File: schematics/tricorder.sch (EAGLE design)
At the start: 70 parts, among them IC1 EADOGM128, U1 V_REG_LDOSMD, U2 CY8C5XXX, U3 M05X2-0.05-SMD, U7 MICROUSB, Y1 XRCGB_XTAL

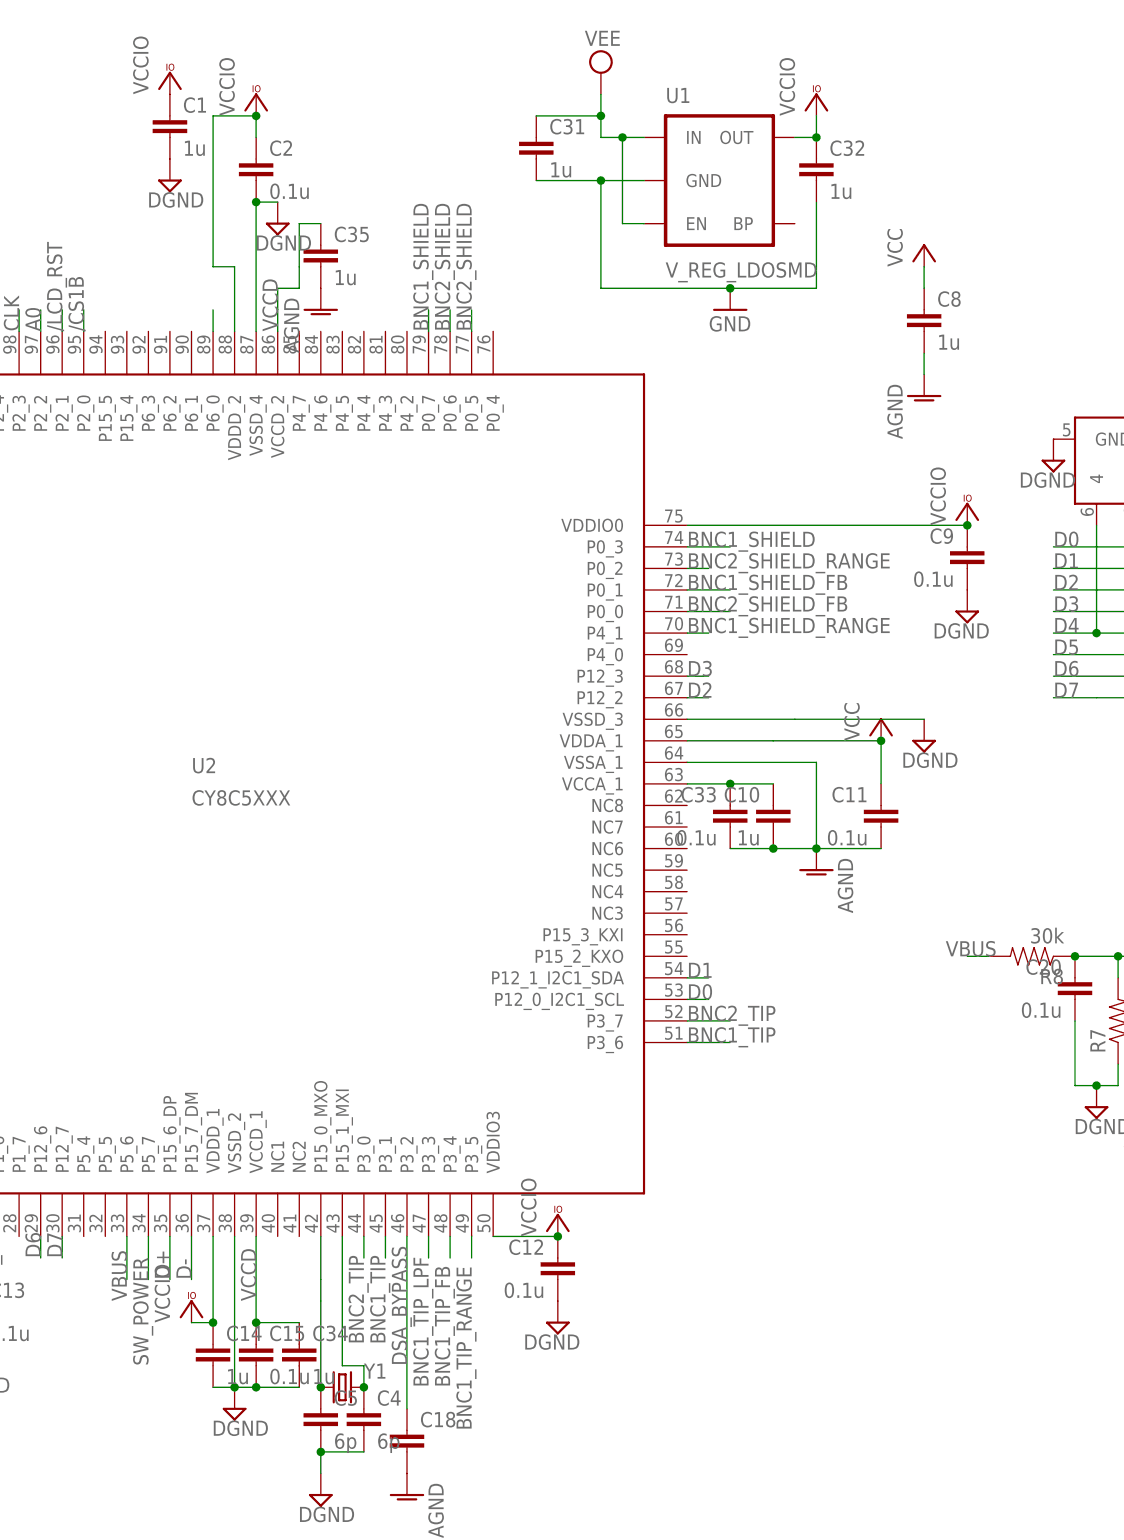
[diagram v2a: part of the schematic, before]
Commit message: Fixed LCD handling in firmware
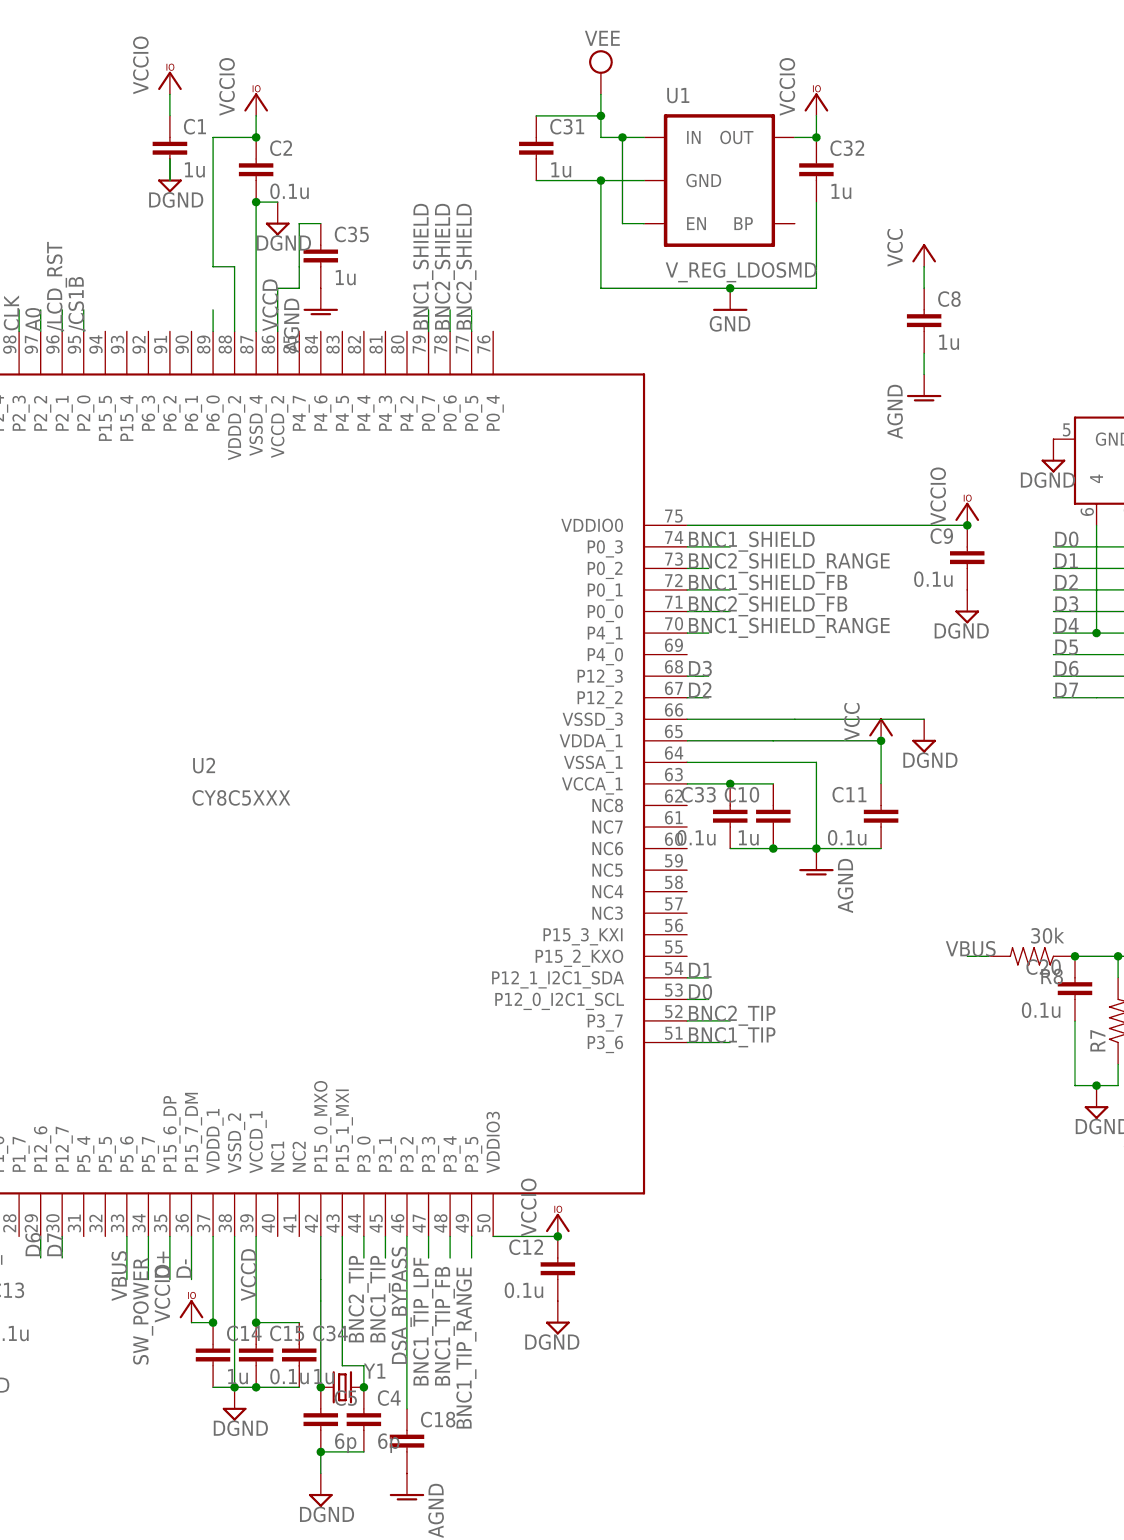
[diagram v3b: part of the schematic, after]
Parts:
- C1, C10, C11, C14, C15, C2, C33, C34, C35, C8, C9: device resistor:C-EUC0603K -> SparkFun-Passives:CAP0603-CAP
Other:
- moved on the sheet: C1
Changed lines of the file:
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@@
 <part name="R1" library="SparkFun-Passives" deviceset="RESISTOR" device="0603-RES" value="22"/>
 <part name="R2" library="SparkFun-Passives" deviceset="RESISTOR" device="0603-RES" value="22"/>
-<part name="C2" library="resistor" deviceset="C-EU" device="C0603K" value="0.1u"/>
-<part name="C10" library="resistor" deviceset="C-EU" device="C0603K" value="1u"/>
-<part name="C11" library="resistor" deviceset="C-EU" device="C0603K" value="0.1u"/>
-<part name="C8" library="resistor" deviceset="C-EU" device="C0603K" value="1u"/>
-<part name="C1" library="resistor" deviceset="C-EU" device="C0603K" value="1u"/>
+<part name="C2" library="SparkFun-Passives" deviceset="CAP" device="0603-CAP" value="0.1u"/>
+<part name="C10" library="SparkFun-Passives" deviceset="CAP" device="0603-CAP" value="1u"/>
+<part name="C11" library="SparkFun-Passives" deviceset="CAP" device="0603-CAP" value="0.1u"/>
+<part name="C8" library="SparkFun-Passives" deviceset="CAP" device="0603-CAP" value="1u"/>
+<part name="C1" library="SparkFun-Passives" deviceset="CAP" device="0603-CAP" value="1u"/>
 <part name="C6" library="resistor" deviceset="C-EU" device="C0603K" value="0.1u"/>
 <part name="C13" library="resistor" deviceset="C-EU" device="C0603K" value="0.1u"/>
 <part name="C12" library="resistor" deviceset="C-EU" device="C0603K" value="0.1u"/>
-<part name="C9" library="resistor" deviceset="C-EU" device="C0603K" value="0.1u"/>
+<part name="C9" library="SparkFun-Passives" deviceset="CAP" device="0603-CAP" value="0.1u"/>
 <part name="U3" library="nickparts" deviceset="M05X2-0.05-SMD" device=""/>
 <part name="GND8" library="supply1" deviceset="GND" device=""/>
@@
 <part name="C4" library="SparkFun-Passives" deviceset="CAP" device="0603-CAP" value="6p"/>
 <part name="C5" library="SparkFun-Passives" deviceset="CAP" device="0603-CAP" value="6p"/>
-<part name="C15" library="resistor" deviceset="C-EU" device="C0603K" value="0.1u"/>
-<part name="C14" library="resistor" deviceset="C-EU" device="C0603K" value="1u"/>
+<part name="C15" library="SparkFun-Passives" deviceset="CAP" device="0603-CAP" value="0.1u"/>
+<part name="C14" library="SparkFun-Passives" deviceset="CAP" device="0603-CAP" value="1u"/>
 <part name="AGND2" library="supply1" deviceset="AGND" device=""/>
 <part name="AGND3" library="supply1" deviceset="AGND" device=""/>
@@
 <part name="U$4" library="nickparts" deviceset="BNC" device=""/>
 <part name="U$11" library="nickparts" deviceset="BNC" device=""/>
-<part name="C33" library="resistor" deviceset="C-EU" device="C0603K" value="0.1u"/>
-<part name="C34" library="resistor" deviceset="C-EU" device="C0603K" value="1u"/>
-<part name="C35" library="resistor" deviceset="C-EU" device="C0603K" value="1u"/>
+<part name="C33" library="SparkFun-Passives" deviceset="CAP" device="0603-CAP" value="0.1u"/>
+<part name="C34" library="SparkFun-Passives" deviceset="CAP" device="0603-CAP" value="1u"/>
+<part name="C35" library="SparkFun-Passives" deviceset="CAP" device="0603-CAP" value="1u"/>
 <part name="AGND8" library="supply1" deviceset="AGND" device=""/>
 <part name="U$16" library="nickparts" deviceset="CAT4003B" device=""/>
@@
 <instance part="R1" gate="G$1" x="248.92" y="144.78"/>
 <instance part="R2" gate="G$1" x="243.84" y="139.7"/>
-<instance part="C2" gate="G$1" x="111.76" y="241.3"/>
-<instance part="C10" gate="G$1" x="172.72" y="165.1" rot="MR0"/>
-<instance part="C11" gate="G$1" x="185.42" y="165.1" rot="MR0"/>
-<instance part="C8" gate="G$1" x="190.5" y="223.52"/>
-<instance part="C1" gate="G$1" x="101.6" y="246.38"/>
+<instance part="C2" gate="G$1" x="111.76" y="238.76"/>
+<instance part="C10" gate="G$1" x="172.72" y="162.56" rot="MR0"/>
+<instance part="C11" gate="G$1" x="185.42" y="162.56" rot="MR0"/>
+<instance part="C8" gate="G$1" x="190.5" y="220.98"/>
+<instance part="C1" gate="G$1" x="101.6" y="241.3"/>
 <instance part="C6" gate="G$1" x="71.12" y="231.14"/>
 <instance part="C13" gate="G$1" x="78.74" y="106.68"/>
 <instance part="C12" gate="G$1" x="147.32" y="111.76" rot="MR0"/>
-<instance part="C9" gate="G$1" x="195.58" y="195.58" rot="MR0"/>
+<instance part="C9" gate="G$1" x="195.58" y="193.04" rot="MR0"/>
 <instance part="U3" gate="G$1" x="246.38" y="233.68"/>
 <instance part="GND8" gate="1" x="236.22" y="226.06"/>
@@
 <instance part="C4" gate="G$1" x="124.46" y="91.44"/>
 <instance part="C5" gate="G$1" x="119.38" y="91.44"/>
-<instance part="C15" gate="G$1" x="111.76" y="101.6"/>
-<instance part="C14" gate="G$1" x="106.68" y="101.6"/>
+<instance part="C15" gate="G$1" x="111.76" y="99.06"/>
+<instance part="C14" gate="G$1" x="106.68" y="99.06"/>
 <instance part="AGND2" gate="VR1" x="190.5" y="213.36"/>
 <instance part="AGND3" gate="VR1" x="177.8" y="157.48" rot="MR0"/>
@@
 <instance part="U$4" gate="G$1" x="55.88" y="55.88" rot="R90"/>
 <instance part="U$11" gate="G$1" x="55.88" y="12.7" rot="R90"/>
-<instance part="C33" gate="G$1" x="167.64" y="165.1" rot="MR0"/>
-<instance part="C34" gate="G$1" x="116.84" y="101.6"/>
-<instance part="C35" gate="G$1" x="119.38" y="231.14"/>
+<instance part="C33" gate="G$1" x="167.64" y="162.56" rot="MR0"/>
+<instance part="C34" gate="G$1" x="116.84" y="99.06"/>
+<instance part="C35" gate="G$1" x="119.38" y="228.6"/>
 <instance part="AGND8" gate="VR1" x="119.38" y="223.52"/>
 <instance part="U$16" gate="G$1" x="363.22" y="121.92" rot="R90"/>
@@
 <segment>
 <pinref part="C8" gate="G$1" pin="2"/>
-<wire x1="190.5" y1="215.9" x2="190.5" y2="218.44" width="0.1524" layer="91"/>
 <pinref part="AGND2" gate="VR1" pin="AGND"/>
+<wire x1="190.5" y1="218.44" x2="190.5" y2="215.9" width="0.1524" layer="91"/>
 </segment>
 <segment>
@@
 <pinref part="C1" gate="G$1" pin="2"/>
 <pinref part="SUPPLY6" gate="G$1" pin="DGND"/>
+<wire x1="101.6" y1="241.3" x2="101.6" y2="238.76" width="0.1524" layer="91"/>
 </segment>
 <segment>
@@
 <wire x1="109.22" y1="220.98" x2="109.22" y2="228.6" width="0.1524" layer="91"/>
 <wire x1="109.22" y1="228.6" x2="106.68" y2="228.6" width="0.1524" layer="91"/>
-<wire x1="106.68" y1="228.6" x2="106.68" y2="246.38" width="0.1524" layer="91"/>
-<wire x1="106.68" y1="246.38" x2="111.76" y2="246.38" width="0.1524" layer="91"/>
+<wire x1="106.68" y1="228.6" x2="106.68" y2="243.84" width="0.1524" layer="91"/>
+<wire x1="106.68" y1="243.84" x2="111.76" y2="243.84" width="0.1524" layer="91"/>
 <pinref part="C2" gate="G$1" pin="1"/>
-<wire x1="111.76" y1="246.38" x2="111.76" y2="243.84" width="0.1524" layer="91"/>
 <pinref part="VCC6" gate="G$1" pin="VCCIO"/>
-<junction x="111.76" y="246.38"/>
+<junction x="111.76" y="243.84"/>
+<wire x1="111.76" y1="243.84" x2="111.76" y2="246.38" width="0.1524" layer="91"/>
 </segment>
 <segment>
 <pinref part="C1" gate="G$1" pin="1"/>
 <pinref part="VCC8" gate="G$1" pin="VCCIO"/>
+<wire x1="101.6" y1="248.92" x2="101.6" y2="246.38" width="0.1524" layer="91"/>
 </segment>
 <segment>
@@
 <segment>
 <pinref part="C8" gate="G$1" pin="1"/>
-<wire x1="190.5" y1="228.6" x2="190.5" y2="226.06" width="0.1524" layer="91"/>
 <pinref part="P+2" gate="VCC" pin="VCC"/>
-</segment>
-<segment>
+<wire x1="190.5" y1="226.06" x2="190.5" y2="228.6" width="0.1524" layer="91"/>
+</segment>
+<segment>
